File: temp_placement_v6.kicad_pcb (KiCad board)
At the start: 4 copper layers, 120 x 170 mm, 33 parts, among them Q1 IKW40N120H3, Q2 IKW40N120H3

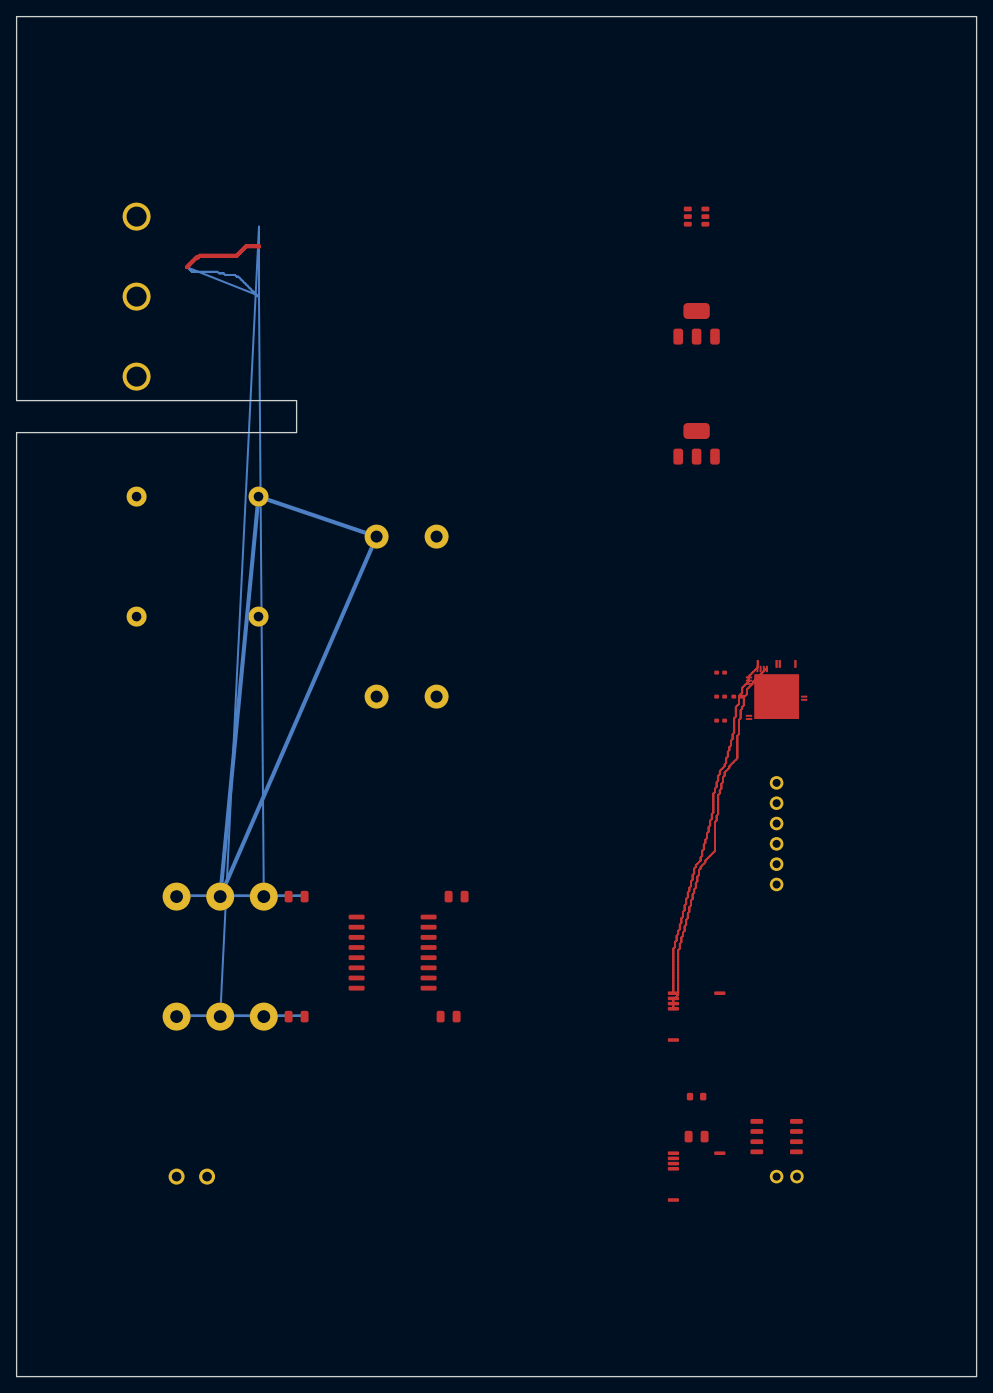
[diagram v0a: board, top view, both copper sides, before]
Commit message: Major Cleanup: JAX Removal, Legacy Purge, and Structural Flattening
What:
- Removed JAX dependencies from the core placement and routing pipeline.
- Purged over 100 legacy files including 'ml/', 'topological/', 'router_v7/', and unused 'routing/' packages.
- Flattened the monorepo structure by removing the redundant 'src/' directory across all packages.
- Ported 'wirelength.py' to NumPy and standardized 'losses/' infrastructure.

Why:
- The project has moved from JAX-based differentiable optimization to a discrete Benders-V6 geometric approach.
- The 5-level deep directory nesting was identified as an anti-pattern and hindered maintainability.
- Consolidated the codebase to focus on the active, stable production pipeline.

How:
- Refactored 'spectral.py', 'state.py', 'base.py', and 'losses/wirelength.py' to use NumPy/SciPy.
- Batch removed obsolete optimization and experimental scripts.
- Physically moved package source code out of 'src/' and updated all 'pyproject.toml' (hatch/pytest/ruff) configurations.
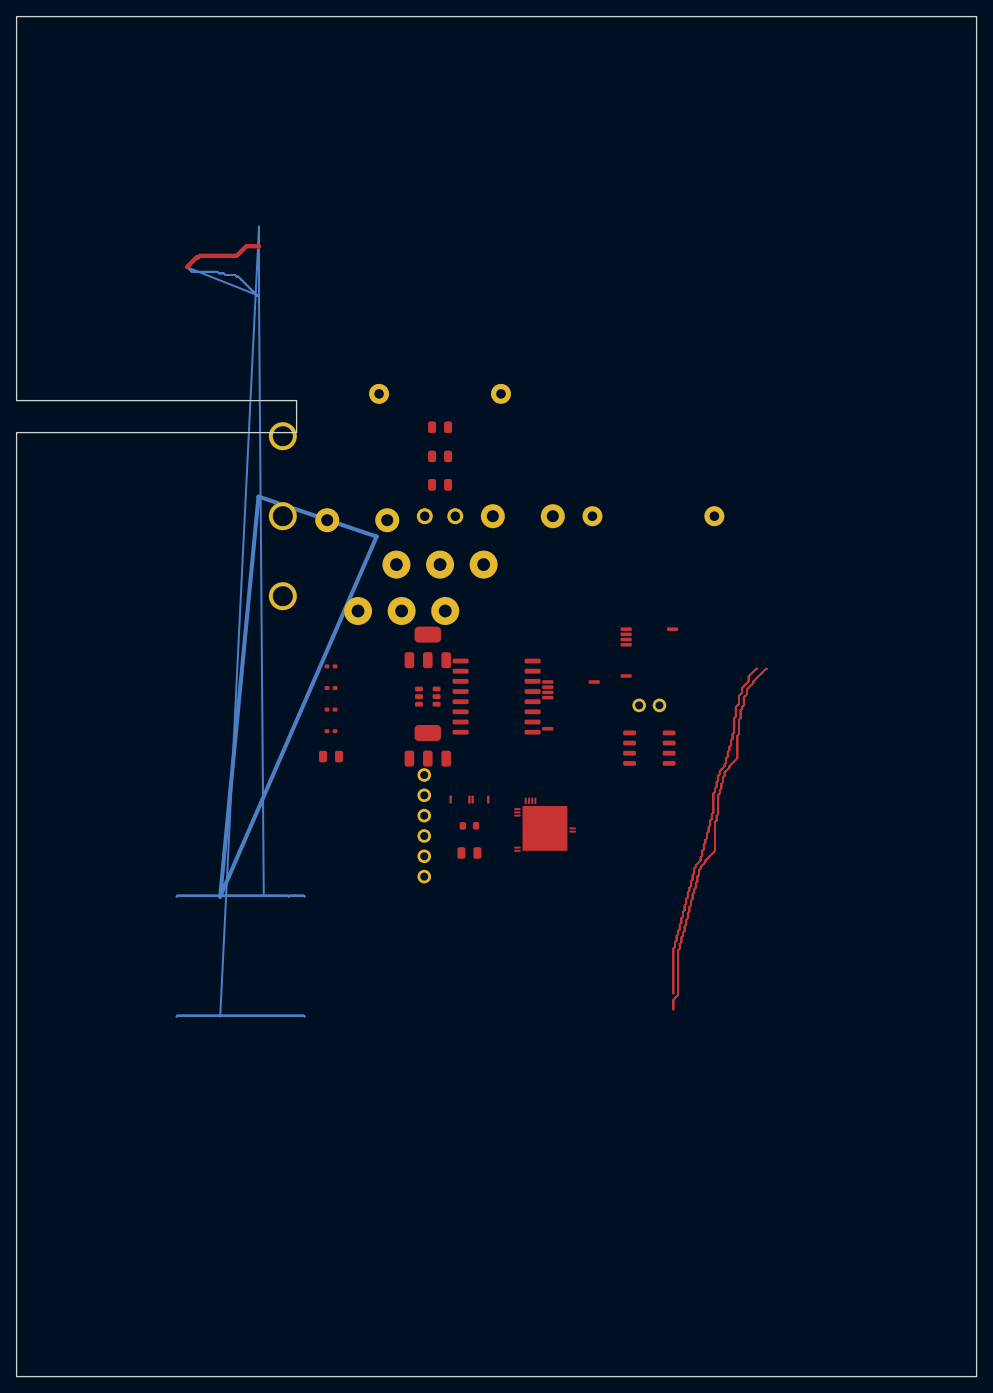
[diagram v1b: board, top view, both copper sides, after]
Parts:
- moved MH4 113.7 mm to (35.3, 83.9)
- moved MH2 104.0 mm to (47.3, 83.9)
- moved MH3 89.7 mm to (43.3, 83.9)
- moved J_COIL 88.2 mm to (51.0, 62.5)
- moved MH1 80.5 mm to (39.3, 77.8)
- moved R_GATE_L 68.8 mm to (52.9, 58.5)
- moved U_BUCK 68.8 mm to (51.4, 85.0)
- moved J_NTC 61.4 mm to (77.8, 86.1)
- moved MAX31865 61.0 mm to (69.3, 86.1)
- moved C_BOOT 58.7 mm to (52.9, 51.3)
- moved D2 58.3 mm to (72.0, 62.5)
- moved R_GATE_H 57.9 mm to (52.9, 55.0)
- moved Q2 55.5 mm to (42.7, 74.3)
- moved U_LDO_3V3 52.6 mm to (51.4, 80.4)
- moved U_OPAMP_CT 51.1 mm to (79.1, 91.4)
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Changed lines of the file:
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@@
   (net 26 "USB_D-")
   (footprint "Connector_IEC:IEC_C14_Male" (layer "F.Cu")
-    (at 15.0 25.0)
+    (at 33.279998779296875 52.45000076293945 0.0)
     (property "Reference" "J_AC_IN")
     (property "Value" "IEC_C14")
@@
   )
   (footprint "Diode_THT:D_DO-201AD_P15.24mm_Horizontal" (layer "F.Cu")
-    (at 15.0 60.0)
+    (at 45.310000305175784 47.15999984741211 0.0)
     (property "Reference" "D1")
     (property "Value" "1N5408")
@@
   )
   (footprint "Diode_THT:D_DO-201AD_P15.24mm_Horizontal" (layer "F.Cu")
-    (at 15.0 75.0)
+    (at 71.97999847412109 62.45000076293945 0.0)
     (property "Reference" "D2")
     (property "Value" "1N5408")
@@
   )
   (footprint "Capacitor_THT:CP_Radial_D18.0mm_P7.50mm" (layer "F.Cu")
-    (at 45.0 65.0)
+    (at 38.83000183105469 62.95000076293945 0.0)
     (property "Reference" "C_BUS1")
     (property "Value" "330uF/400V")
@@
   )
   (footprint "Capacitor_THT:CP_Radial_D18.0mm_P7.50mm" (layer "F.Cu")
-    (at 45.0 85.0)
+    (at 59.529998779296875 62.45000076293945 0.0)
     (property "Reference" "C_BUS2")
     (property "Value" "330uF/400V")
@@
   )
   (footprint "Package_TO_SOT_THT:TO-247-3_Horizontal_TabDown" (layer "F.Cu")
-    (at 20.0 110.0)
+    (at 47.48000030517578 68.5 0.0)
     (property "Reference" "Q1")
     (property "Value" "IKW40N120H3")
@@
   )
   (footprint "Package_TO_SOT_THT:TO-247-3_Horizontal_TabDown" (layer "F.Cu")
-    (at 20.0 125.0)
+    (at 42.68000106811523 74.30000305175781 0.0)
     (property "Reference" "Q2")
     (property "Value" "IKW40N120H3")
@@
   )
   (footprint "Package_SO:SOIC-16W_7.5x10.3mm_P1.27mm" (layer "F.Cu")
-    (at 47.0 117.0)
+    (at 60.0 85.0 0.0)
     (property "Reference" "U_GATE")
     (property "Value" "UCC21550")
@@
   )
   (footprint "Capacitor_SMD:C_0805_2012Metric" (layer "F.Cu")
-    (at 55.0 110.0)
+    (at 52.93000030517578 51.33000183105469 0.0)
     (property "Reference" "C_BOOT")
     (property "Value" "10uF")
@@
   )
   (footprint "Capacitor_SMD:C_0805_2012Metric" (layer "F.Cu")
-    (at 54.0 125.0)
+    (at 39.29999923706055 92.49749755859375 0.0)
     (property "Reference" "C_VCC")
     (property "Value" "10uF")
@@
   )
   (footprint "Resistor_SMD:R_0805_2012Metric" (layer "F.Cu")
-    (at 35.0 110.0)
+    (at 52.93000030517578 54.97999954223633 0.0)
     (property "Reference" "R_GATE_H")
     (property "Value" "4.7R")
@@
   )
   (footprint "Resistor_SMD:R_0805_2012Metric" (layer "F.Cu")
-    (at 35.0 125.0)
+    (at 52.93000030517578 58.529998779296875 0.0)
     (property "Reference" "R_GATE_L")
     (property "Value" "4.7R")
@@
   )
   (footprint "Connector_Phoenix_MC:PhoenixContact_MCV_1,5_2-G-3.81_1x02_P3.81mm_Vertical" (layer "F.Cu")
-    (at 20.0 145.0)
+    (at 51.02500030517578 62.45000076293945 0.0)
     (property "Reference" "J_COIL")
     (property "Value" "Coil")
@@
   )
   (footprint "Package_TO_SOT_SMD:SOT-23-6" (layer "F.Cu")
-    (at 85.0 25.0)
+    (at 51.400001525878906 85.0 0.0)
     (property "Reference" "U_BUCK")
     (property "Value" "LMR51430")
@@
   )
   (footprint "Package_TO_SOT_SMD:SOT-223-3_TabPin2" (layer "F.Cu")
-    (at 85.0 40.0)
+    (at 51.400001525878906 80.44999847412109 0.0)
     (property "Reference" "U_LDO_3V3")
     (property "Value" "AMS1117-3.3")
@@
   )
   (footprint "Package_TO_SOT_SMD:SOT-223-3_TabPin2" (layer "F.Cu")
-    (at 85.0 55.0)
+    (at 51.400001525878906 92.7500015258789 0.0)
     (property "Reference" "U_LDO_5V")
     (property "Value" "AMS1117-5.0")
@@
   )
   (footprint "Package_DFN_QFN:QFN-56-1EP_7x7mm_P0.4mm_EP5.6x5.6mm" (layer "F.Cu")
-    (at 95.0 85.0)
+    (at 66.04499816894531 101.47500152587891 0.0)
     (property "Reference" "U_MCU")
     (property "Value" "ESP32-S3-WROOM-1")
@@
   )
   (footprint "Capacitor_SMD:C_0402_1005Metric" (layer "F.Cu")
-    (at 88.0 82.0)
+    (at 39.29999923706055 81.22750091552734 0.0)
     (property "Reference" "C_MCU_1")
     (property "Value" "100nF")
@@
   )
   (footprint "Capacitor_SMD:C_0402_1005Metric" (layer "F.Cu")
-    (at 88.0 85.0)
+    (at 39.29999923706055 83.92749786376953 0.0)
     (property "Reference" "C_MCU_2")
     (property "Value" "100nF")
@@
   )
   (footprint "Capacitor_SMD:C_0402_1005Metric" (layer "F.Cu")
-    (at 88.0 88.0)
+    (at 39.29999923706055 89.32749938964844 0.0)
     (property "Reference" "C_MCU_3")
     (property "Value" "100nF")
@@
   )
   (footprint "Capacitor_SMD:C_0402_1005Metric" (layer "F.Cu")
-    (at 90.14999999999998 85.0)
+    (at 39.29999923706055 86.62750244140625 0.0)
     (property "Reference" "C_MCU_4")
     (property "Value" "10uF")
@@
   )
   (footprint "Connector_USB:USB_C_Receptacle_HRO_TYPE-C-31-M-12" (layer "F.Cu")
-    (at 95.0 80.91500000000002)
+    (at 56.60499954223633 97.87999725341797 0.0)
     (property "Reference" "J_USB")
     (property "Value" "USB_C")
@@
   )
   (footprint "Connector_PinHeader_2.54mm:PinHeader_1x06_P2.54mm_Vertical" (layer "F.Cu")
-    (at 95.0 95.78500000000003)
+    (at 50.95500183105469 94.80000152587891 0.0)
     (property "Reference" "J_DEBUG")
     (property "Value" "Debug")
@@
   )
   (footprint "Package_SO:TSSOP-20_4.4x6.5mm_P0.65mm" (layer "F.Cu")
-    (at 85.0 125.0)
+    (at 79.08999633789062 79.49749755859375 0.0)
     (property "Reference" "U_CT")
     (property "Value" "MAX31865")
@@
   )
   (footprint "Resistor_SMD:R_0805_2012Metric" (layer "F.Cu")
-    (at 85.0 140.0)
+    (at 56.60499954223633 104.55000305175781 0.0)
     (property "Reference" "R_BURDEN")
     (property "Value" "33R")
@@
   )
   (footprint "Capacitor_SMD:C_0603_1608Metric" (layer "F.Cu")
-    (at 85.0 135.0)
+    (at 56.60499954223633 101.1500015258789 0.0)
     (property "Reference" "C_CT_FILT")
     (property "Value" "100pF")
@@
   )
   (footprint "Package_SO:SOIC-8_3.9x4.9mm_P1.27mm" (layer "F.Cu")
-    (at 95.0 140.0)
+    (at 79.08999633789062 91.44750213623047 0.0)
     (property "Reference" "U_OPAMP_CT")
     (property "Value" "LM358")
@@
   )
   (footprint "Package_SO:TSSOP-20_4.4x6.5mm_P0.65mm" (layer "F.Cu")
-    (at 85.0 145.0)
+    (at 69.30000305175781 86.09750366210938 0.0)
     (property "Reference" "MAX31865")
     (property "Value" "MAX31865")
@@
   )
   (footprint "Connector_PinHeader_2.54mm:PinHeader_1x02_P2.54mm_Vertical" (layer "F.Cu")
-    (at 95.0 145.0)
+    (at 77.81999633789063 86.09750366210938 0.0)
     (property "Reference" "J_NTC")
     (property "Value" "NTC")
@@
   )
   (footprint "MountingHole:MountingHole_3.2mm_M3" (layer "F.Cu")
-    (at 5 5)
+    (at 39.29999923706055 77.77749633789062 0.0)
     (property "Reference" "MH1")
     (property "Value" "MountingHole_3.2mm_M3")
@@
   )
   (footprint "MountingHole:MountingHole_3.2mm_M3" (layer "F.Cu")
-    (at 115 5)
+    (at 47.29999923706055 83.92749786376953 0.0)
     (property "Reference" "MH2")
     (property "Value" "MountingHole_3.2mm_M3")
@@
   )
   (footprint "MountingHole:MountingHole_3.2mm_M3" (layer "F.Cu")
-    (at 5 165)
+    (at 43.29999923706055 83.92749786376953 0.0)
     (property "Reference" "MH3")
     (property "Value" "MountingHole_3.2mm_M3")
@@
   )
   (footprint "MountingHole:MountingHole_3.2mm_M3" (layer "F.Cu")
-    (at 115 165)
+    (at 35.29999923706055 83.92749786376953 0.0)
     (property "Reference" "MH4")
     (property "Value" "MountingHole_3.2mm_M3")
